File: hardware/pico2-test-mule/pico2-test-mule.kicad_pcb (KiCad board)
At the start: 2 copper layers, 52.5 x 42 mm, 71 parts, among them J2 SPEAKER, J4 POWER, J5 EXT_CAP, J6 RAILS, J7 AUX, J8 MOTOR, Q1 DMN2991UDA-7B, Q10 SS8050, Q11 SS8050, Q12 SS8050, Q13 SS8050, Q2 DMN2991UDA-7B, Q3 NST847BPDP6T5G, Q4 NST847BPDP6T5G, Q5 DMN2991UDA-7B, Q6 DMN2991UDA-7B, Q7 DMN2991UDA-7B, Q8 DMN2991UDA-7B, Q9 SS8050, U1 NCS2220AMUT1G, U2 AP63203WU, U5 MAX98357AEWL+T, U6 MD9927, U7 PICO

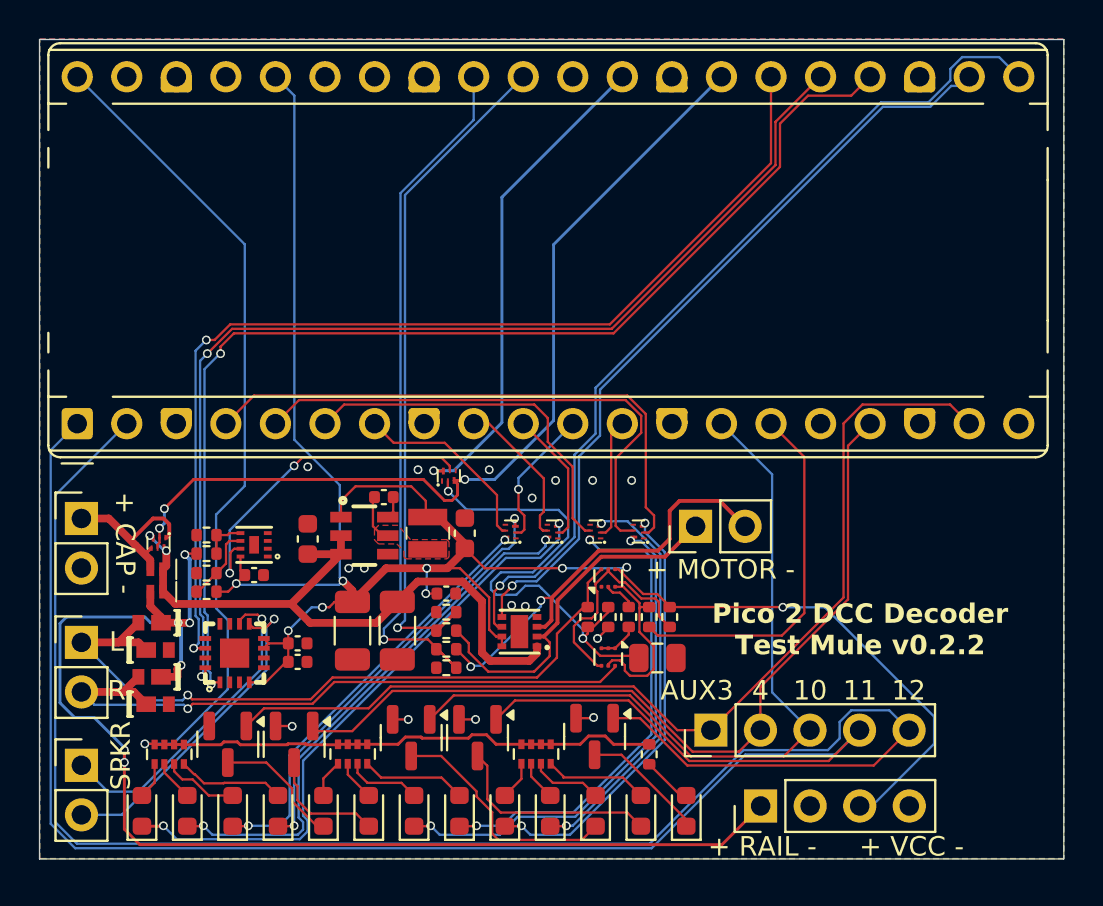
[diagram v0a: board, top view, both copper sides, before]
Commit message: fix: combine left side headers
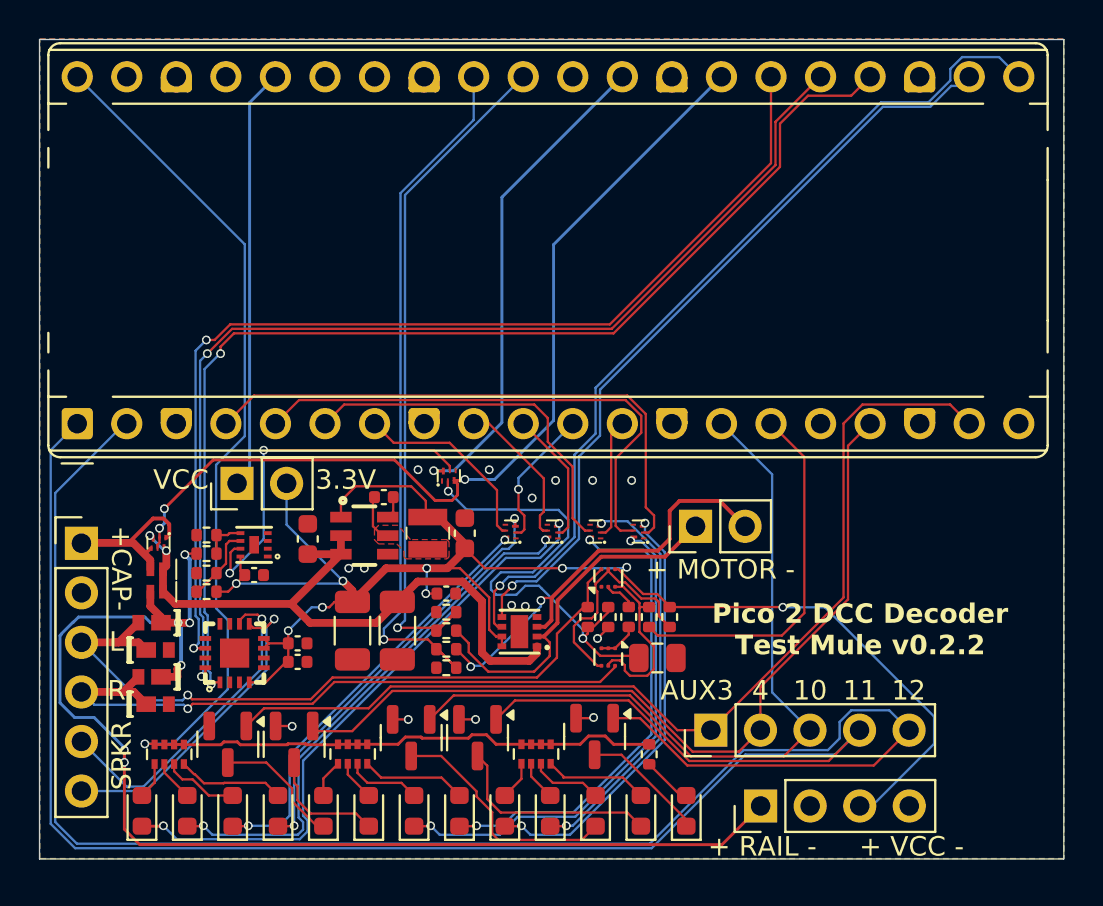
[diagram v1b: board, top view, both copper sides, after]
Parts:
- removed the J2 at (90.3, 75.8)
- removed J6: RAILS, Connector_PinHeader_2.54mm:PinHeader_1x02_P2.54mm_Vertical
- added J1: SPEAKER, Connector_PinHeader_2.54mm:PinHeader_1x06_P2.54mm_Vertical, F.Cu at (90.3, 64.5)
- J5: value EXT_CAP -> VCC
- moved J5 8.18 mm to (98.3, 61.4), turned to 90 degrees
- renumbered C20 to C10, C5 to C3, C7 to C4, C8 to C5, C3 to C6, C18 to C7, C17 to C8, C19 to C9, D12 to D10, D13 to D11, D14 to D12, D5 to D13, D15 to D14, D16 to D15, D17 to D16, D18 to D17, D6 to D18, D7 to D3, D8 to D4, D9 to D5, D10 to D6, D3 to D7, D4 to D8, D11 to D9, J4 to J2, J7 to J3, J8 to J4, Q6 to Q10, Q5 to Q11, Q8 to Q12, Q7 to Q13, Q9 to Q2, Q10 to Q3, Q2 to Q4, Q11 to Q5, Q12 to Q6, Q3 to Q7, Q13 to Q8, Q4 to Q9, R13 to R10, R16 to R11, R17 to R12, R18 to R13, R19 to R14, R7 to R5, R8 to R6, R5 to R7, R11 to R8, R12 to R9, U7 to U3, U5 to U4, U6 to U5
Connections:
- J5 pad 1: /CAP+ -> Net-(J5-Pin_1)
- J5 pad 2: GND -> +3.3V
- U3 pad 36: +3.3V -> Net-(J5-Pin_1)
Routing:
- net Net-(J5-Pin_1): track 0.00 -> 21.7 mm
- net +3.3V: track 103.9 -> 82.8 mm
- net Net-(Q1B-G2): track 17.1 -> 18.8 mm
- net /CAP_ENABLE: track 46.7 -> 47.6 mm
- net /CAP+: track 9.00 -> 8.50 mm
- net /SPEAKER_P: track 16.9 -> 16.4 mm
- net GND: vias 16 -> 15
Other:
- board text added: "+CAP-"
- board text added: "3.3V"
- board text added: "VCC"
- board text removed: "+ CAP -"

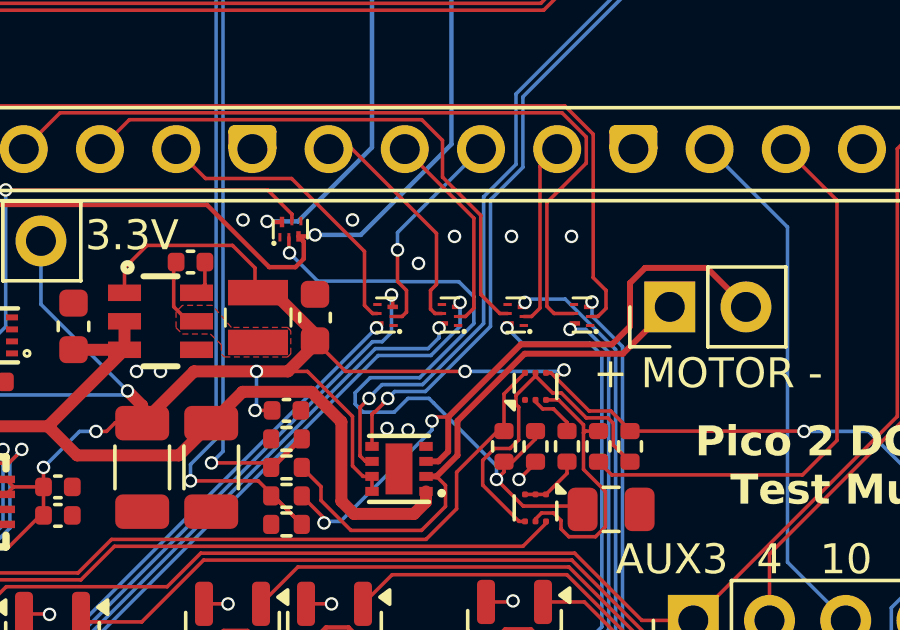
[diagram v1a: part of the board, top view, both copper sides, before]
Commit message: chore: rearrange labels
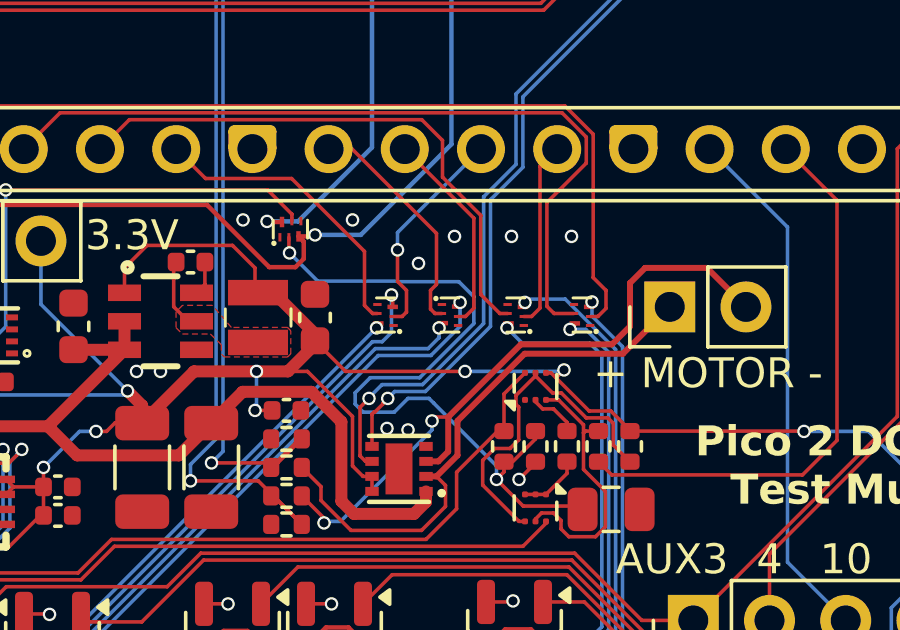
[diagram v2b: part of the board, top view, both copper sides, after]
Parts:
- turned Q10 to -90 degrees
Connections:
- Q10 pad 2: /GPIO7 -> /GPIO6
- Q10 pad 3: /LAMP_FRONT -> /LAMP_REAR
- Q10 pad 5: /GPIO6 -> /GPIO7
- Q10 pad 6: /LAMP_REAR -> /LAMP_FRONT
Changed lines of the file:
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@@
 	(footprint "pico2-test-mule:X2-DFN0806-6_L0.8-W0.6_X2-DFN0806-6"
 		(layer "F.Cu")
-		(at 114.449771 63.87 90)
+		(at 114.449771 63.87 -90)
 		(property "Reference" "Q10"
 			(at 0 -4.27 90)
@@
 		)
 		(property "LCSC" "C2937136"
-			(at 0 0 90)
+			(at 0 0 270)
 			(unlocked yes)
 			(layer "F.Fab")
@@
 		)
 		(property "Height" "0.4"
-			(at 0 0 90)
+			(at 0 0 270)
 			(unlocked yes)
 			(layer "F.Fab")
@@
 		(attr smd)
 		(fp_line
-			(start 0.57 -0.3)
-			(end 0.57 0.3)
+			(start -0.57 0.3)
+			(end -0.57 -0.3)
 			(stroke
 				(width 0.1)
@@
 		)
 		(fp_line
-			(start -0.57 0.3)
-			(end -0.57 -0.3)
+			(start 0.57 -0.3)
+			(end 0.57 0.3)
 			(stroke
 				(width 0.1)
@@
 		)
 		(pad "1" smd rect
-			(at -0.35 0.27 90)
+			(at -0.35 0.27 270)
 			(size 0.1 0.28)
 			(layers "F.Cu" "F.Mask" "F.Paste")
@@
 		)
 		(pad "2" smd rect
-			(at -0.05 0.27 90)
+			(at -0.05 0.27 270)
 			(size 0.1 0.28)
 			(layers "F.Cu" "F.Mask" "F.Paste")
-			(net 41 "/GPIO7")
+			(net 43 "/GPIO6")
 			(pinfunction "G1")
 			(pintype "passive")
 		)
 		(pad "3" smd rect
-			(at 0.27 0.24 90)
+			(at 0.27 0.24 270)
 			(size 0.15 0.35)
 			(layers "F.Cu" "F.Mask" "F.Paste")
-			(net 6 "/LAMP_FRONT")
+			(net 7 "/LAMP_REAR")
 			(pinfunction "D2")
 			(pintype "passive")
 		)
 		(pad "4" smd rect
-			(at 0.35 -0.27 90)
+			(at 0.35 -0.27 270)
 			(size 0.1 0.28)
 			(layers "F.Cu" "F.Mask" "F.Paste")
@@
 		)
 		(pad "5" smd rect
-			(at 0.05 -0.27 90)
+			(at 0.05 -0.27 270)
 			(size 0.1 0.28)
 			(layers "F.Cu" "F.Mask" "F.Paste")
-			(net 43 "/GPIO6")
+			(net 41 "/GPIO7")
 			(pinfunction "G2")
 			(pintype "passive")
 		)
 		(pad "6" smd rect
-			(at -0.28 -0.24 90)
+			(at -0.28 -0.24 270)
 			(size 0.15 0.35)
 			(layers "F.Cu" "F.Mask" "F.Paste")
-			(net 7 "/LAMP_REAR")
+			(net 6 "/LAMP_FRONT")
 			(pinfunction "D1")
 			(pintype "passive")
